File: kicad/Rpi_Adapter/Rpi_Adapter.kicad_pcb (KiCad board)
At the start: 2 copper layers, 62.4 x 32.1 mm, 49 parts, among them P1 CONN_02X20, P2 CONN_01X08

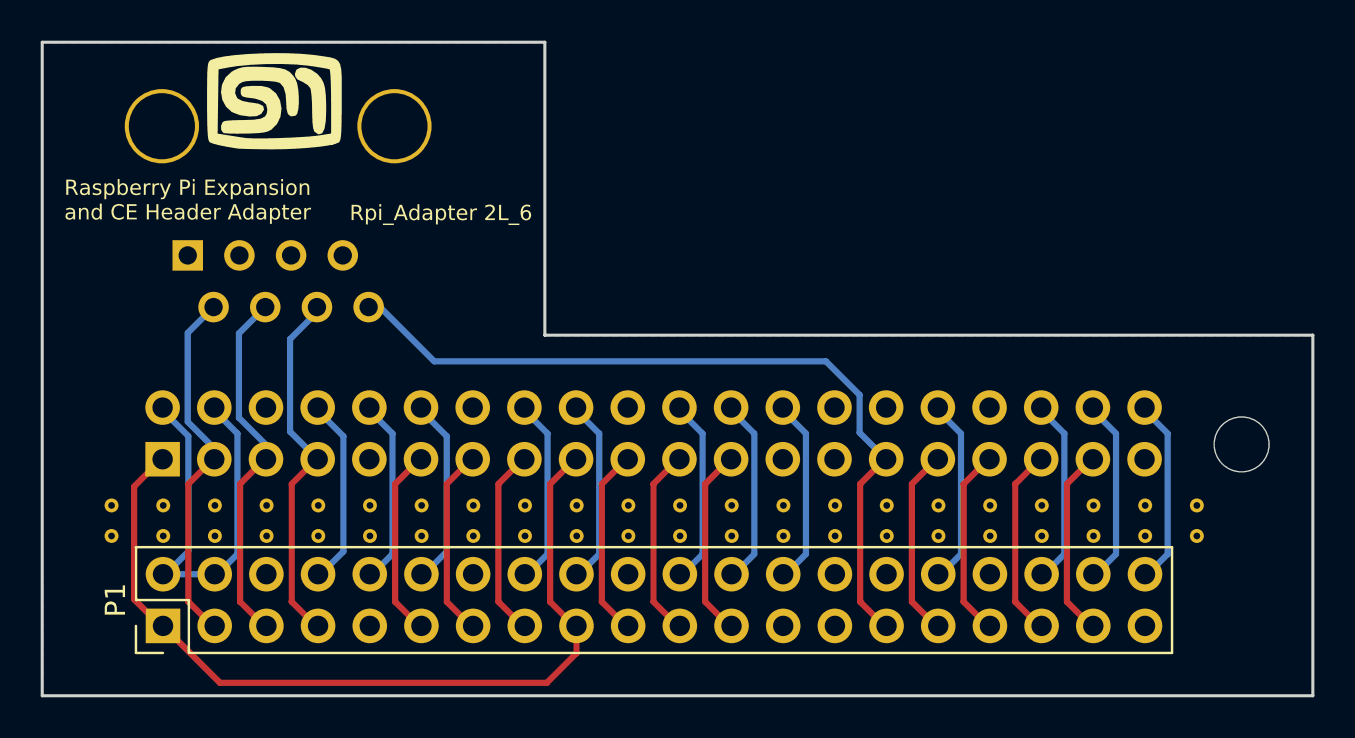
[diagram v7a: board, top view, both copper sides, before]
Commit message: Radically reduced the size of the board
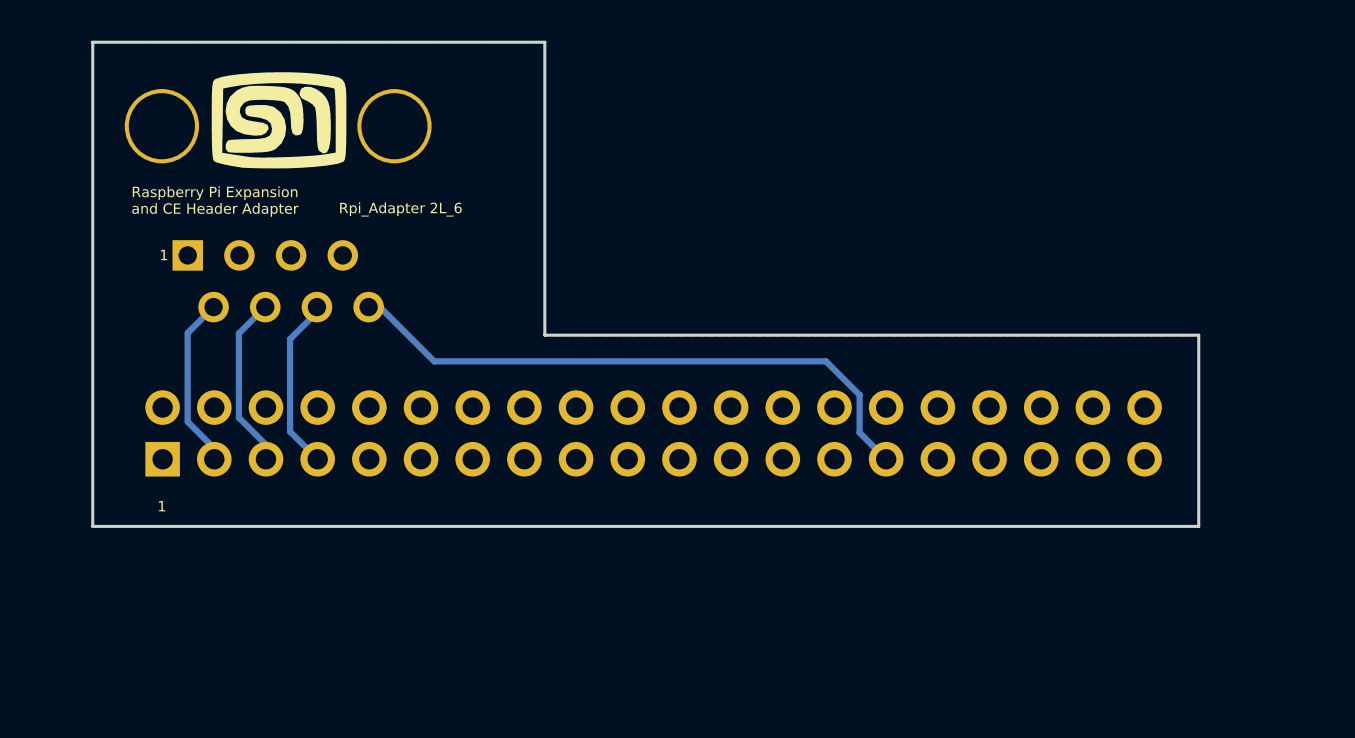
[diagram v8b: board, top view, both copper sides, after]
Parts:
- removed ? (x44): Stitch, Rpi_Adapter_Footprints:Stitch
- removed MNT**: MountingHole_2.7mm_M2.5, Mounting_Holes:MountingHole_2.7mm_M2.5
- removed P1: CONN_02X20, Pin_Headers:Pin_Header_Straight_2x20_Pitch2.54mm
- moved G*** 0.97 mm to (170.1, 29.5)
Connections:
- MCU1 pad 10: /UART0_Rx -> (no net)
- MCU1 pad 11: /GPIO_17 -> (no net)
- MCU1 pad 12: /GPIO_18 -> (no net)
- MCU1 pad 13: /GPIO_27 -> (no net)
- MCU1 pad 15: /GPIO_22 -> (no net)
- MCU1 pad 16: /GPIO_23 -> (no net)
- MCU1 pad 18: /GPIO_24 -> (no net)
- MCU1 pad 19: /SPI0_MOSI -> (no net)
- MCU1 pad 21: /SPI0_MISO -> (no net)
- MCU1 pad 22: /GPIO_25 -> (no net)
- MCU1 pad 23: /SPI0_SCLK -> (no net)
- MCU1 pad 24: /SPI0_CS0 -> (no net)
- MCU1 pad 26: /SPI0_CS1 -> (no net)
- MCU1 pad 31: /GPIO_6 -> (no net)
- MCU1 pad 32: /GPIO_12 -> (no net)
- MCU1 pad 33: /GPIO_13 -> (no net)
- MCU1 pad 35: /GPIO_19 -> (no net)
- MCU1 pad 36: /GPIO_16 -> (no net)
- MCU1 pad 37: /GPIO_26 -> (no net)
- MCU1 pad 38: /GPIO_20 -> (no net)
- MCU1 pad 40: /GPIO_21 -> (no net)
- MCU1 pad 8: /UART0_Tx -> (no net)
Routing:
- net /3V3: track 42.1 -> 0.00 mm
- net /5V: track 21.1 -> 0.00 mm
- net /GPIO_18: track 9.35 -> 0.00 mm
- net /UART0_Tx: track 9.35 -> 0.00 mm
- net /GPIO_5: track 38.9 -> 29.6 mm
- net /GPIO_27: track 9.30 -> 0.00 mm
- net /SPI0_SCLK: track 9.30 -> 0.00 mm
- net /SPI0_MISO: track 9.30 -> 0.00 mm
- net /GPIO_6: track 9.30 -> 0.00 mm
- net /GPIO_4: track 17.9 -> 8.59 mm
- net /GPIO_26: track 9.30 -> 0.00 mm
- net /GPIO_22: track 9.30 -> 0.00 mm
- net /GPIO_19: track 9.30 -> 0.00 mm
- net /SPI0_MOSI: track 9.30 -> 0.00 mm
- net /I2C1_SCL: track 17.9 -> 8.57 mm
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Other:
- board size 62.4 x 32.1 mm -> 54.4 x 23.8 mm
- board text added: "1"
- board text removed: "TL2C Connector"
